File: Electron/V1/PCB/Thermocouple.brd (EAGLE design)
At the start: 95.9 x 34.6 mm, 30 parts, among them U1 MAX31855K, U2 ELECTRONDUALNAMED, U3 24LC512

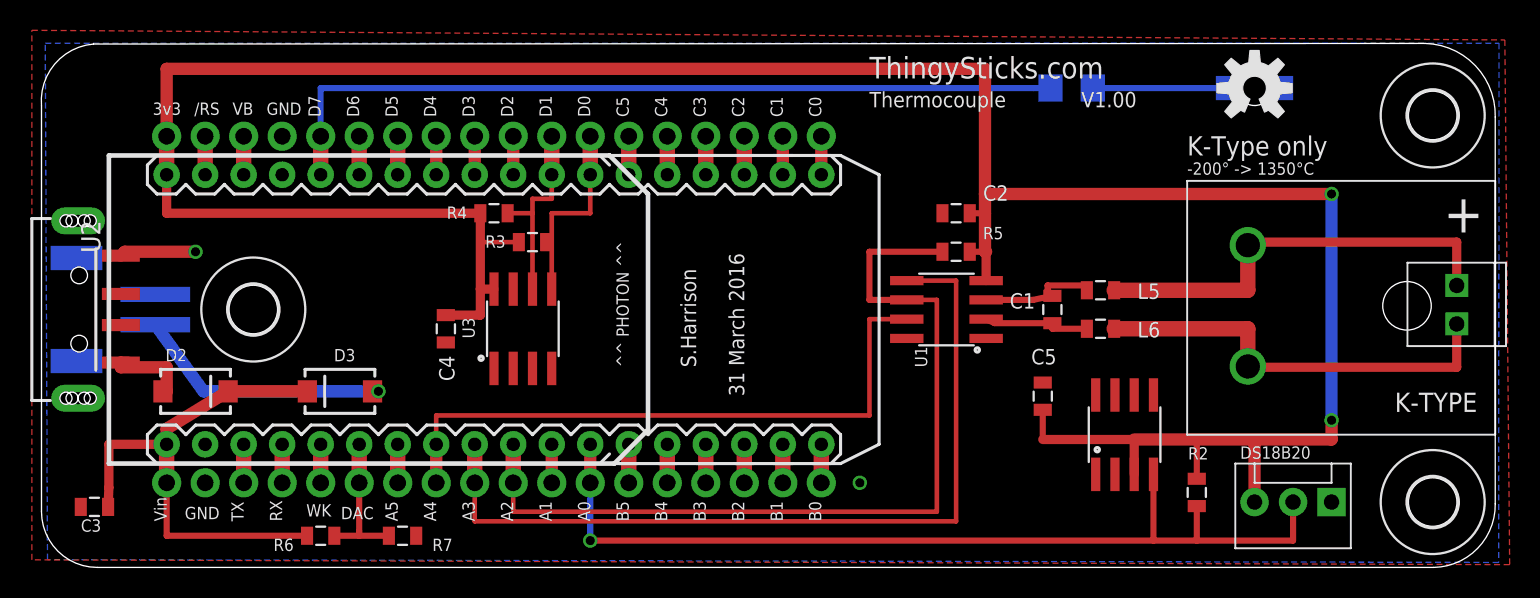
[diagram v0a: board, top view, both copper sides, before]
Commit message: Updated to V1.1 * Removed DS18B20 to focus on thermocouple only. * Added solder pads to allow select using A0/1/2 and B0-5 for stackable sensors with single photon/electron. * Removed battery connector and diodes. * Minor change to board dimensions. * Moved OSH Logo + LED down a little for board changes. Added DirtyPCB Images. Added pdfs of PCB/Schematics for V1.1
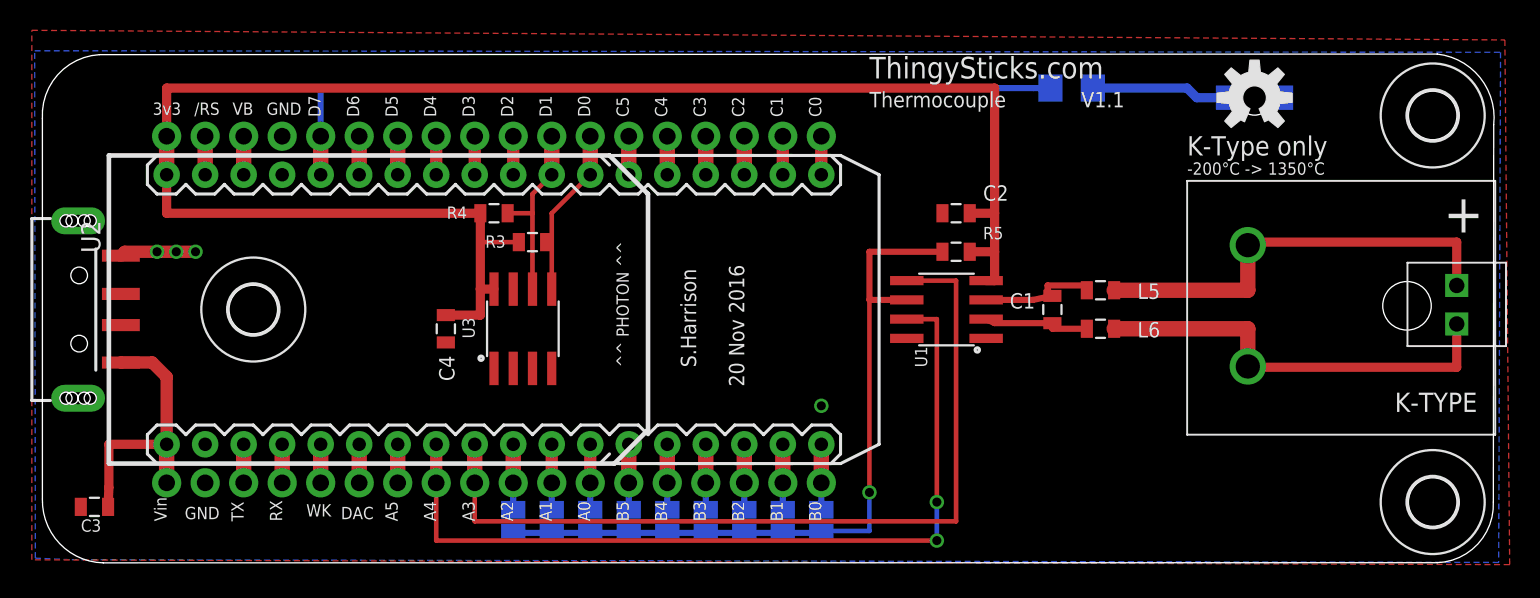
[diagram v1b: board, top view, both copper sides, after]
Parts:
- removed C5: 0.1uF, SparkFun-Passives:0805
- removed D2, D3: (no value), SparkFun-DiscreteSemi:SMA-DIODE
- removed JP2: (no value), SparkFun-Connectors:MOLEX-1X3
- removed JP3: (no value), SparkFun-Connectors:JST-2-SMD
- removed R2, R6, R7: 10k, SparkFun-Resistors:0805
- removed U$1: DS1820SOIC, DS1820-SOIC:DS18B20_SOIC
- added SJ1, SJ2, SJ3, SJ4, SJ5, SJ6, SJ7, SJ8, SJ9: (no value), jumper:SJ
- moved D1 0.63 mm to (95.2, 26.7)
- moved LOGO1 0.63 mm to (95.2, 26.7)
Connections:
- removed net N$1: CONN1.VBUS1, D2.A
- removed net VIN_MONITOR: R6.1, R7.2, U2.DAC, U2.DAC_1
- new net N$30: SJ1.2, U2.A2, U2.A2_1
- net 3.3V: no longer C5.2, JP2.3, R2.2, U$1.VCC
- net 5V: now also CONN1.VBUS1; no longer D2.C, D3.C, R6.2
- net DQ: now also SJ3.2; no longer JP2.2, R2.1, U$1.DQ
- net GND: no longer C5.1, JP2.1, JP3.1, R7.1, U$1.GND
- net N$29: now also U2.DAC, U2.DAC_1; no longer D3.A, JP3.2
- net N$3: now also SJ2.2
- net N$31: now also SJ9.2
- net N$33: now also SJ8.2
- net N$35: now also SJ7.2
- net N$36: now also SJ6.2
- net N$37: now also SJ5.2
- net N$38: now also SJ4.2
- net SS: now also SJ1.1, SJ2.1, SJ3.1, SJ4.1, SJ5.1, SJ6.1, SJ7.1, SJ8.1, SJ9.1; no longer U2.A2, U2.A2_1
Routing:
- net 3.3V: track 183.7 -> 114.4 mm, vias 2 -> 0
- net DQ: track 61.9 -> 4.32 mm, vias 1 -> 0
- net MISO: track 41.8 -> 58.5 mm, vias 0 -> 2
- net 5V: track 36.8 -> 20.9 mm
- net N$29: track 17.4 -> 2.54 mm, vias 1 -> 0
- net SS: track 61.3 -> 49.4 mm, vias 0 -> 1
- net VIN_MONITOR: track 9.63 -> 0.00 mm
- net N$1: track 5.63 -> 0.00 mm
- net N$30: track 0.00 -> 4.32 mm
- net N$38: track 2.54 -> 4.32 mm
- net N$37: track 2.54 -> 4.32 mm
- net N$36: track 2.54 -> 4.32 mm
- net N$35: track 2.54 -> 4.32 mm
- net N$33: track 2.54 -> 4.32 mm
- net N$31: track 2.54 -> 4.32 mm
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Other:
- board size 95.9 x 34.6 mm -> 95.8 x 33.6 mm
- board text added: "-200°C -> 1350°C"
- board text added: "20 Nov 2016"
- board text added: "3v3"
- board text added: "A0"
- board text added: "A1"
- board text added: "A2"
- board text added: "B0"
- board text added: "B1"
- board text added: "B2"
- board text added: "B3"
- board text added: "B4"
- board text added: "B5"
- board text added: "C0"
- board text added: "D0"
- board text added: "GND"
- board text added: "V1.1"
- board text added: "Vin"
- board text removed: "-200° -> 1350°C"
- board text removed: "31 March 2016"
- board text removed: "Battery. 3.7v LiPol Disconnect USB First"
- board text removed: "DS18B20"
- board text removed: "V1.00"
